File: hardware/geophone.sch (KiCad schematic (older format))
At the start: 27 parts, among them P1 CONN_01X02, P2 CONN_01X02, P3 CONN_01X02, P4 CONN_01X05, P5 CONN_01X02, P6 CONN_01X02, P7 CONN_01X02, U1 ICL7660, U2 IC741, U3 IC741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

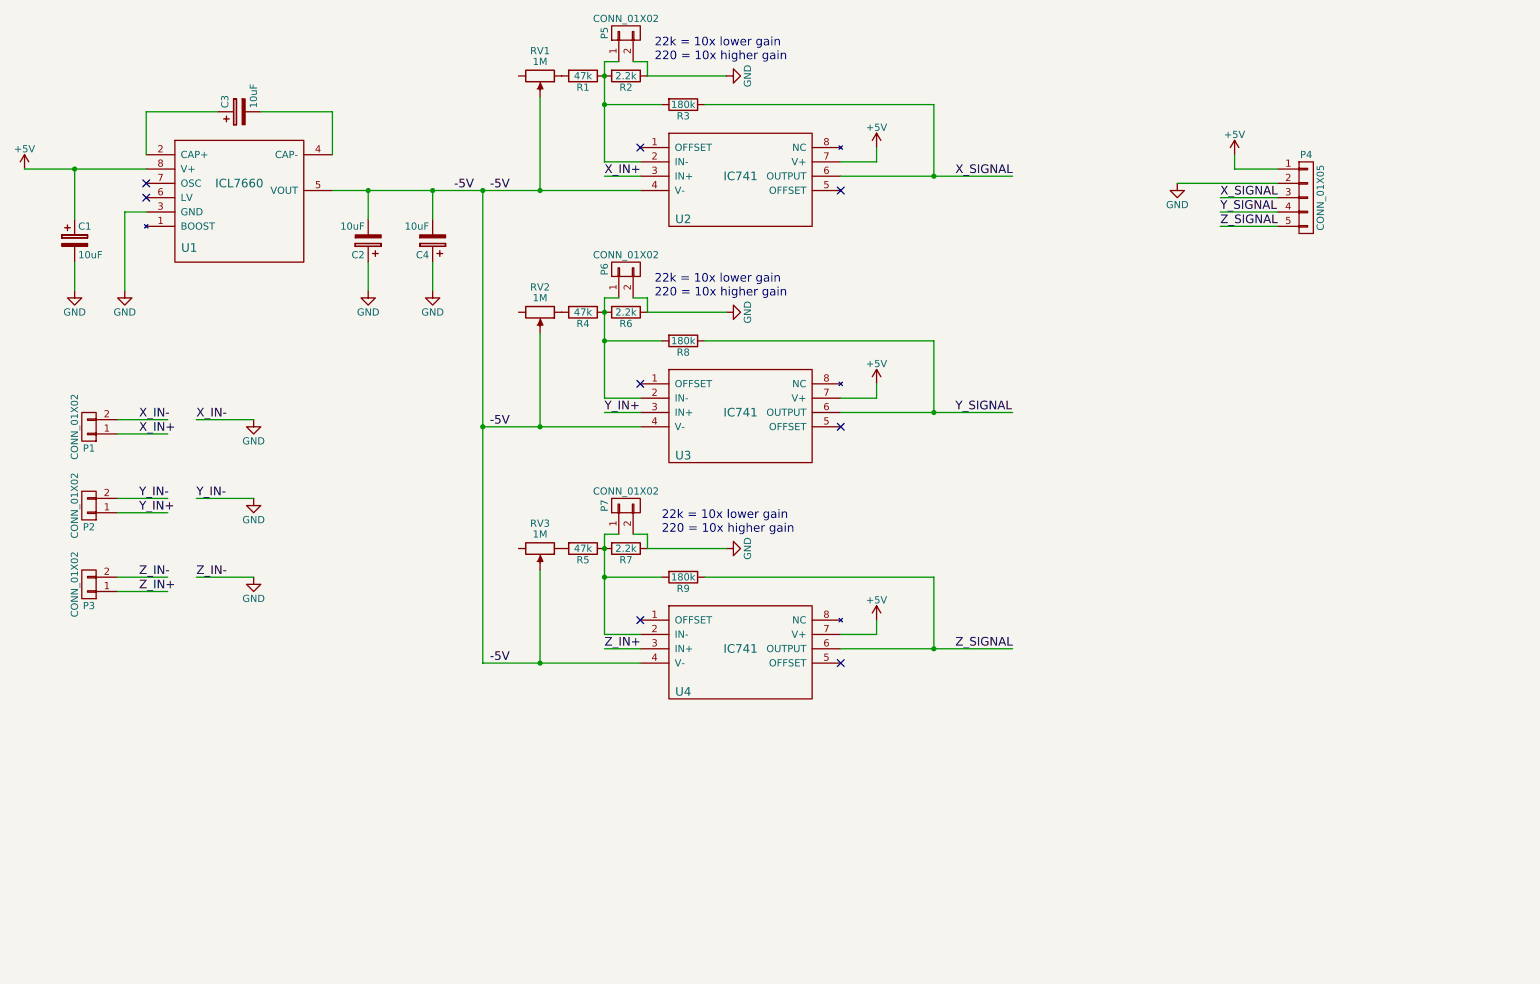
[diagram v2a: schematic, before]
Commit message: Adding the feather to the board.
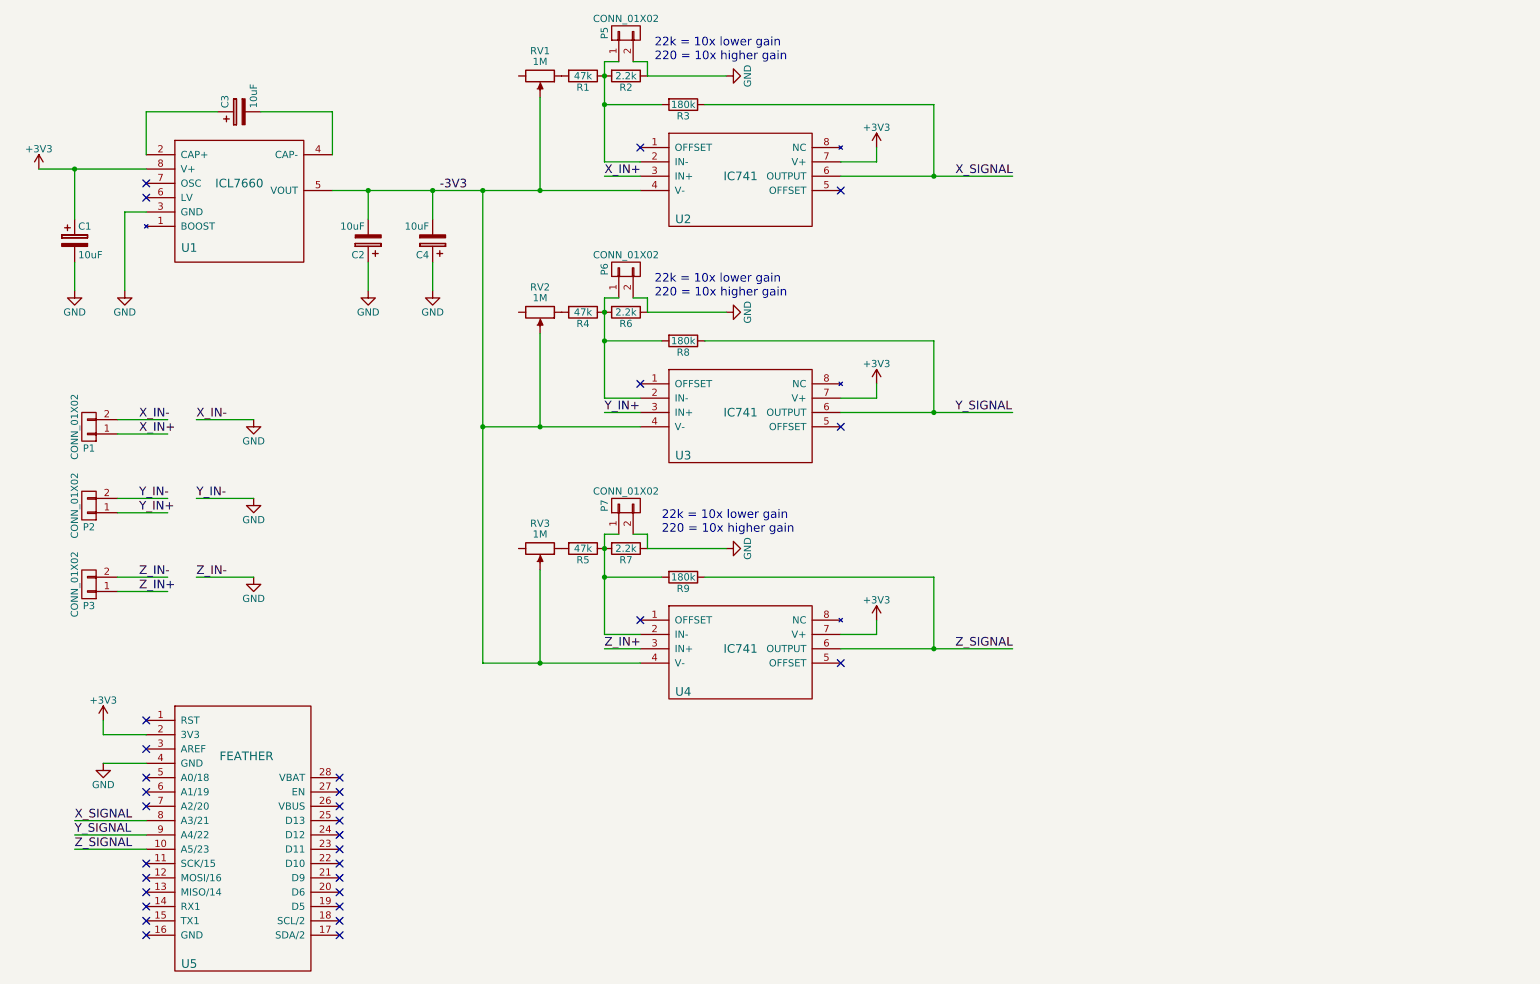
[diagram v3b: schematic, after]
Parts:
- removed P4: CONN_01X05, Socket_Strips:Socket_Strip_Straight_1x05, symbol CONN_01X05
- added U5: FEATHER, hardware:feather, symbol FEATHER
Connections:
- net labels added: +3V3, -3V3
- net labels removed: +5V, -5V
- no-connect marks 8 -> 31
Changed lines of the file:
@@
 LIBS:ic741
 LIBS:mcp413x
+LIBS:feather
 LIBS:geophone-cache
 EELAYER 25 0
@@
 	-1   0    0    1
 $EndComp
-$Comp
-L +5V #PWR04
-U 1 1 588A3C21
-P 600 1700
-F 0 "#PWR04" H 600 1550 50  0001 C CNN
-F 1 "+5V" H 600 1840 50  0000 C CNN
-F 2 "" H 600 1700 50  0000 C CNN
-F 3 "" H 600 1700 50  0000 C CNN
-	1    600  1700
-	1    0    0    -1
-$EndComp
-$Comp
-L +5V #PWR05
-U 1 1 588A3C63
-P 6550 1550
-F 0 "#PWR05" H 6550 1400 50  0001 C CNN
-F 1 "+5V" H 6550 1690 50  0000 C CNN
-F 2 "" H 6550 1550 50  0000 C CNN
-F 3 "" H 6550 1550 50  0000 C CNN
-	1    6550 1550
-	1    0    0    -1
-$EndComp
 Text Label 7100 1750 0    60   ~ 0
 X_SIGNAL
@@
 X_IN-
 $Comp
-L GND #PWR06
+L GND #PWR04
 U 1 1 588A3E86
 P 2200 3450
-F 0 "#PWR06" H 2200 3200 50  0001 C CNN
+F 0 "#PWR04" H 2200 3200 50  0001 C CNN
 F 1 "GND" H 2200 3300 50  0000 C CNN
 F 2 "" H 2200 3450 50  0000 C CNN
@@
 	3000 2550 3000 2350
 Wire Wire Line
-	600  1700 1450 1700
+	700  1700 1450 1700
 Wire Wire Line
 	950  1700 950  2050
@@
 Connection ~ 4650 1250
 $Comp
-L GND #PWR07
+L GND #PWR05
 U 1 1 588A407A
 P 5500 1050
-F 0 "#PWR07" H 5500 800 50  0001 C CNN
+F 0 "#PWR05" H 5500 800 50  0001 C CNN
 F 1 "GND" H 5500 900 50  0000 C CNN
 F 2 "" H 5500 1050 50  0000 C CNN
@@
 Connection ~ 4200 1850
 Connection ~ 6950 1750
-Text Label 3850 1850 0    60   ~ 0
--5V
 Text Notes 5000 950  0    60   ~ 0
 22k = 10x lower gain\n220 = 10x higher gain
@@
 Y_IN-
 $Comp
-L GND #PWR08
+L GND #PWR06
 U 1 1 588A8349
 P 2200 4000
-F 0 "#PWR08" H 2200 3750 50  0001 C CNN
+F 0 "#PWR06" H 2200 3750 50  0001 C CNN
 F 1 "GND" H 2200 3850 50  0000 C CNN
 F 2 "" H 2200 4000 50  0000 C CNN
@@
 Z_IN-
 $Comp
-L GND #PWR09
+L GND #PWR07
 U 1 1 588A84D6
 P 2200 4550
-F 0 "#PWR09" H 2200 4300 50  0001 C CNN
+F 0 "#PWR07" H 2200 4300 50  0001 C CNN
 F 1 "GND" H 2200 4400 50  0000 C CNN
 F 2 "" H 2200 4550 50  0000 C CNN
@@
 	0    1    1    0
 $EndComp
-$Comp
-L +5V #PWR010
-U 1 1 588A8BEE
-P 6550 3200
-F 0 "#PWR010" H 6550 3050 50  0001 C CNN
-F 1 "+5V" H 6550 3340 50  0000 C CNN
-F 2 "" H 6550 3200 50  0000 C CNN
-F 3 "" H 6550 3200 50  0000 C CNN
-	1    6550 3200
-	1    0    0    -1
-$EndComp
 Text Label 7100 3400 0    60   ~ 0
 Y_SIGNAL
@@
 Connection ~ 4650 2900
 $Comp
-L GND #PWR011
+L GND #PWR08
 U 1 1 588A8C06
 P 5500 2700
-F 0 "#PWR011" H 5500 2450 50  0001 C CNN
+F 0 "#PWR08" H 5500 2450 50  0001 C CNN
 F 1 "GND" H 5500 2550 50  0000 C CNN
 F 2 "" H 5500 2700 50  0000 C CNN
@@
 Connection ~ 4200 3500
 Connection ~ 6950 3400
-Text Label 3850 3500 0    60   ~ 0
--5V
 Text Notes 5000 2600 0    60   ~ 0
 22k = 10x lower gain\n220 = 10x higher gain
@@
 	0    1    1    0
 $EndComp
-$Comp
-L +5V #PWR012
-U 1 1 588A8DBB
-P 6550 4850
-F 0 "#PWR012" H 6550 4700 50  0001 C CNN
-F 1 "+5V" H 6550 4990 50  0000 C CNN
-F 2 "" H 6550 4850 50  0000 C CNN
-F 3 "" H 6550 4850 50  0000 C CNN
-	1    6550 4850
-	1    0    0    -1
-$EndComp
 Text Label 7100 5050 0    60   ~ 0
 Z_SIGNAL
@@
 Connection ~ 4650 4550
 $Comp
-L GND #PWR013
+L GND #PWR09
 U 1 1 588A8DD3
 P 5500 4350
-F 0 "#PWR013" H 5500 4100 50  0001 C CNN
+F 0 "#PWR09" H 5500 4100 50  0001 C CNN
 F 1 "GND" H 5500 4200 50  0000 C CNN
 F 2 "" H 5500 4350 50  0000 C CNN
@@
 Connection ~ 4200 5150
 Connection ~ 6950 5050
-Text Label 3850 5150 0    60   ~ 0
--5V
 Text Notes 5050 4250 0    60   ~ 0
 22k = 10x lower gain\n220 = 10x higher gain
@@
 Connection ~ 3450 1850
 $Comp
-L GND #PWR014
+L GND #PWR010
 U 1 1 588A9390
 P 3450 2550
-F 0 "#PWR014" H 3450 2300 50  0001 C CNN
+F 0 "#PWR010" H 3450 2300 50  0001 C CNN
 F 1 "GND" H 3450 2400 50  0000 C CNN
 F 2 "" H 3450 2550 50  0000 C CNN
@@
 Wire Wire Line
 	3450 2550 3450 2350
-$Comp
-L CONN_01X05 P4
-U 1 1 588A95CF
-P 9550 1900
-F 0 "P4" H 9550 2200 50  0000 C CNN
-F 1 "CONN_01X05" V 9650 1900 50  0000 C CNN
-F 2 "Socket_Strips:Socket_Strip_Straight_1x05" H 9550 1900 50  0001 C CNN
-F 3 "" H 9550 1900 50  0000 C CNN
-	1    9550 1900
-	1    0    0    -1
-$EndComp
-$Comp
-L +5V #PWR015
-U 1 1 588A9728
-P 9050 1600
-F 0 "#PWR015" H 9050 1450 50  0001 C CNN
-F 1 "+5V" H 9050 1740 50  0000 C CNN
-F 2 "" H 9050 1600 50  0000 C CNN
-F 3 "" H 9050 1600 50  0000 C CNN
-	1    9050 1600
-	1    0    0    -1
-$EndComp
-Wire Wire Line
-	9350 1700 9050 1700
-Wire Wire Line
-	9050 1700 9050 1600
-Text Label 8950 1900 0    60   ~ 0
-X_SIGNAL
-Text Label 8950 2000 0    60   ~ 0
-Y_SIGNAL
-Text Label 8950 2100 0    60   ~ 0
-Z_SIGNAL
-Wire Wire Line
-	8950 1900 9350 1900
-Wire Wire Line
-	9350 2000 8950 2000
-Wire Wire Line
-	8950 2100 9350 2100
-Wire Wire Line
-	8650 1800 9350 1800
-$Comp
-L GND #PWR016
-U 1 1 588A9FCE
-P 8650 1800
-F 0 "#PWR016" H 8650 1550 50  0001 C CNN
-F 1 "GND" H 8650 1650 50  0000 C CNN
-F 2 "" H 8650 1800 50  0000 C CNN
-F 3 "" H 8650 1800 50  0000 C CNN
-	1    8650 1800
-	1    0    0    -1
-$EndComp
-Text Label 3600 1850 0    60   ~ 0
--5V
+Text Label 3500 1850 0    60   ~ 0
+-3V3
 $Comp
 L CONN_01X02 P5
@@
 Wire Wire Line
 	4950 2600 4950 2700
+$Comp
+L FEATHER U5
+U 1 1 589290E9
+P 2150 5800
+F 0 "U5" H 1750 4350 60  0000 C CNN
+F 1 "FEATHER" H 2150 5800 60  0000 C CNN
+F 2 "hardware:feather" H 2150 5800 60  0001 C CNN
+F 3 "" H 2150 5800 60  0001 C CNN
+	1    2150 5800
+	1    0    0    -1
+$EndComp
+$Comp
+L +3V3 #PWR012
+U 1 1 589292DD
+P 700 1700
+F 0 "#PWR012" H 700 1550 50  0001 C CNN
+F 1 "+3V3" H 700 1840 50  0000 C CNN
+F 2 "" H 700 1700 50  0000 C CNN
+F 3 "" H 700 1700 50  0000 C CNN
+	1    700  1700
+	1    0    0    -1
+$EndComp
+$Comp
+L +3V3 #PWR013
+U 1 1 589297C8
+P 6550 1550
+F 0 "#PWR013" H 6550 1400 50  0001 C CNN
+F 1 "+3V3" H 6550 1690 50  0000 C CNN
+F 2 "" H 6550 1550 50  0000 C CNN
+F 3 "" H 6550 1550 50  0000 C CNN
+	1    6550 1550
+	1    0    0    -1
+$EndComp
+$Comp
+L +3V3 #PWR014
+U 1 1 58929827
+P 6550 3200
+F 0 "#PWR014" H 6550 3050 50  0001 C CNN
+F 1 "+3V3" H 6550 3340 50  0000 C CNN
+F 2 "" H 6550 3200 50  0000 C CNN
+F 3 "" H 6550 3200 50  0000 C CNN
+	1    6550 3200
+	1    0    0    -1
+$EndComp
+$Comp
+L +3V3 #PWR015
+U 1 1 58929886
+P 6550 4850
+F 0 "#PWR015" H 6550 4700 50  0001 C CNN
+F 1 "+3V3" H 6550 4990 50  0000 C CNN
+F 2 "" H 6550 4850 50  0000 C CNN
+F 3 "" H 6550 4850 50  0000 C CNN
+	1    6550 4850
+	1    0    0    -1
+$EndComp
+$Comp
+L +3V3 #PWR016
+U 1 1 58929C95
+P 1150 5550
+F 0 "#PWR016" H 1150 5400 50  0001 C CNN
+F 1 "+3V3" H 1150 5690 50  0000 C CNN
+F 2 "" H 1150 5550 50  0000 C CNN
+F 3 "" H 1150 5550 50  0000 C CNN
+	1    1150 5550
+	1    0    0    -1
+$EndComp
+Wire Wire Line
+	1450 5650 1150 5650
+Wire Wire Line
+	1150 5650 1150 5550
+Text Label 950  6250 0    60   ~ 0
+X_SIGNAL
+Text Label 950  6350 0    60   ~ 0
+Y_SIGNAL
+Text Label 950  6450 0    60   ~ 0
+Z_SIGNAL
+Wire Wire Line
+	1450 6250 950  6250
+Wire Wire Line
+	950  6350 1450 6350
+Wire Wire Line
+	1450 6450 950  6450
+NoConn ~ 1450 6150
+NoConn ~ 1450 6050
+NoConn ~ 1450 5950
+NoConn ~ 1450 5750
+NoConn ~ 1450 5550
+NoConn ~ 1450 6550
+NoConn ~ 1450 6650
+NoConn ~ 1450 6750
+NoConn ~ 1450 6850
+NoConn ~ 1450 6950
+NoConn ~ 2800 6950
+NoConn ~ 2800 7050
+NoConn ~ 2800 6850
+NoConn ~ 2800 6750
+NoConn ~ 2800 6650
+NoConn ~ 2800 6550
+NoConn ~ 2800 6450
+NoConn ~ 2800 6350
+NoConn ~ 2800 6250
+NoConn ~ 2800 6150
+NoConn ~ 2800 6050
+NoConn ~ 2800 5950
+$Comp
+L GND #PWR019
+U 1 1 5892B4A0
+P 1150 5850
+F 0 "#PWR019" H 1150 5600 50  0001 C CNN
+F 1 "GND" H 1150 5700 50  0000 C CNN
+F 2 "" H 1150 5850 50  0000 C CNN
+F 3 "" H 1150 5850 50  0000 C CNN
+	1    1150 5850
+	1    0    0    -1
+$EndComp
+Wire Wire Line
+	1450 5850 1150 5850
+NoConn ~ 1450 7050
 $EndSCHEMATC

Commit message: New amplifier schematic from Jeff.
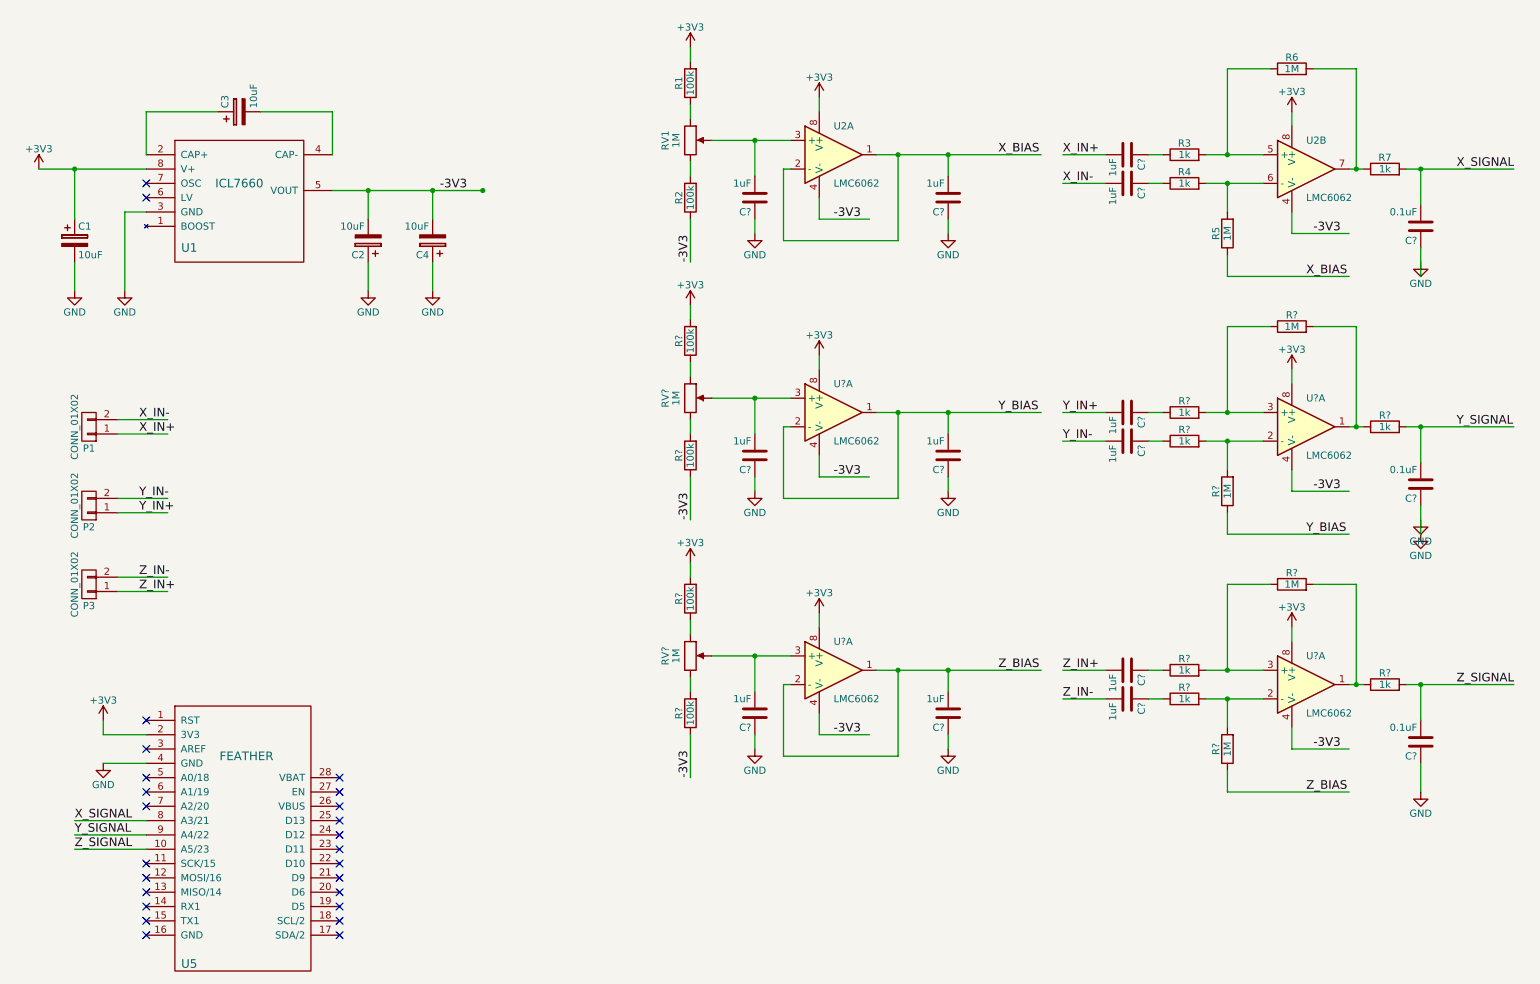
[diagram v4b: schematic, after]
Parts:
- removed P5, P6, P7: CONN_01X02, Socket_Strips:Socket_Strip_Straight_1x02, symbol CONN_01X02
- removed R8, R9: 180k, Resistors_ThroughHole:R_Axial_DIN0207_L6.3mm_D2.5mm_P10.16mm_Horizontal, symbol R
- removed RV2, RV3: 1M, hardware:POT, symbol POT
- removed U2, U3, U4: IC741, Housings_DIP:DIP-8_W7.62mm_LongPads, symbol IC741
- added C? (x12): 1uF, symbol C
- added C? (x3): 0.1uF, symbol C
- added R? (x4): 100k, Resistors_ThroughHole:R_Axial_DIN0207_L6.3mm_D2.5mm_P10.16mm_Horizontal, symbol R
- added R? (x4): 1M, Resistors_ThroughHole:R_Axial_DIN0207_L6.3mm_D2.5mm_P10.16mm_Horizontal, symbol R
- added R? (x6): 1k, Resistors_ThroughHole:R_Axial_DIN0207_L6.3mm_D2.5mm_P10.16mm_Horizontal, symbol R
- added RV? (x2): 1M, hardware:POT, symbol POT
- added U2, U? (x4): LMC6062, symbol LMC6062
- R1: value 47k -> 100k; SPN CF14JT47K0CT-ND -> 2.2KQBK-ND
- R2: value 2.2k -> 100k; SPN 2.2KQBK-ND -> CF14JT180KCT-ND
- R3: value 180k -> 1k; SPN CF14JT180KCT-ND -> 2.2KQBK-ND
- R4: value 47k -> 1k; SPN CF14JT47K0CT-ND -> 2.2KQBK-ND
- R5: value 47k -> 1M; SPN CF14JT47K0CT-ND -> 2.2KQBK-ND
- R6: value 2.2k -> 1M
- R7: value 2.2k -> 1k
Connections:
- net labels added: X_BIAS, Y_BIAS, Z_BIAS
- wire segments 74 -> 161
- no-connect marks 31 -> 25
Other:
- note removed: "22k = 10x lower gain\n220 = 10x higher gain"
